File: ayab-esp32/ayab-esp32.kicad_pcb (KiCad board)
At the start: 2 copper layers, 57 parts, among them J501 USB_C_Receptacle_USB2.0, J601 VIN, Q201 AO3400A, Q502 AO3401A, Q603 AO3401A, U201 ESP32-S3-MINI-1, U301 ULN2003A, U302 ULN2003A, U303 ULN2003A, U501 SRV05-4, U601 XL1509, U602 XL1509, U701 SN74LVC4245

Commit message: add component selection, bom
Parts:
- removed Q603: AO3401A, ayab-esp32:SOT-23
- added BUZZER201: MLT-8530, easyeda2kicad:BUZ-SMD_4P-L8.5-W8.5-P8.50-BR, F.Cu at (-35.3, -30.9)
- added C201: 100n, Capacitor_SMD:C_0603_1608Metric, F.Cu at (221.6, -89.7)
- added C202: 100n, Capacitor_SMD:C_0603_1608Metric, F.Cu at (221.6, -87.2)
- added C203: 100n, Capacitor_SMD:C_0603_1608Metric, F.Cu at (221.6, -84.7)
- added C204: 100n, Capacitor_SMD:C_0603_1608Metric, F.Cu at (221.6, -82.1)
- added C205: 10u, Capacitor_SMD:C_0805_2012Metric, F.Cu at (229.8, -103.7)
- added C301: 100n, Capacitor_SMD:C_0603_1608Metric, F.Cu at (159.8, -100.4)
- added C302: 10u, Capacitor_SMD:C_0805_2012Metric, F.Cu at (159.9, -88.6)
- added C303: 10u, Capacitor_SMD:C_0805_2012Metric, F.Cu at (172.4, -88.6)
- added C304: 10u, Capacitor_SMD:C_0805_2012Metric, F.Cu at (147.4, -88.6)
- added C701: 100n, Capacitor_SMD:C_0603_1608Metric, F.Cu at (288.0, -95.0)
- added C702: 100n, Capacitor_SMD:C_0603_1608Metric, F.Cu at (292.8, -95.0)
- added C703: 100n, Capacitor_SMD:C_0603_1608Metric, F.Cu at (285.1, -73.5)
- added C704: 100n, Capacitor_SMD:C_0603_1608Metric, F.Cu at (285.1, -63.0)
- added D201: LED_YEL, Diode_SMD:D_0805_2012Metric, F.Cu at (215.3, -86.2)
- added D202: LED_GRN, Diode_SMD:D_0805_2012Metric, F.Cu at (215.3, -83.6)
- added D203: LED_RED, Diode_SMD:D_0805_2012Metric, F.Cu at (215.3, -81.0)
- added D204: SS54, Diode_SMD:D_SMA, F.Cu at (-36.5, -23.4)
- added D601: SS54, Diode_SMD:D_SMA, F.Cu at (397.3, -85.4)
- added FID101: Fiducial, Fiducial:Fiducial_0.5mm_Mask1.5mm, F.Cu at (82.2, -68.3)
- added FID102: Fiducial, Fiducial:Fiducial_0.5mm_Mask1.5mm, F.Cu at (82.2, -65.3)
- added FID103: Fiducial, Fiducial:Fiducial_0.5mm_Mask1.5mm, F.Cu at (82.2, -62.2)
- added H101: M3, MountingHole:MountingHole_2.2mm_M2_DIN965_Pad, F.Cu at (83.3, -77.9)
- added H102: M3, MountingHole:MountingHole_2.2mm_M2_DIN965_Pad, F.Cu at (83.3, -72.5)
- added H103: M3, MountingHole:MountingHole_2.2mm_M2_DIN965_Pad, F.Cu at (88.7, -77.9)
- added H104: M3, MountingHole:MountingHole_2.2mm_M2_DIN965_Pad, F.Cu at (88.7, -72.5)
- added H105: M3, MountingHole:MountingHole_2.2mm_M2_DIN965_Pad, F.Cu at (94.0, -77.9)
- added H106: M3, MountingHole:MountingHole_2.2mm_M2_DIN965_Pad, F.Cu at (94.0, -72.5)
- added H107: M3, MountingHole:MountingHole_2.2mm_M2_DIN965_Pad, F.Cu at (99.4, -77.9)
- added H108: M3, MountingHole:MountingHole_2.2mm_M2_DIN965_Pad, F.Cu at (99.4, -72.5)
- added J201: SPARE1, Connector_PinSocket_2.54mm:PinSocket_1x04_P2.54mm_Vertical, F.Cu at (-47.5, -33.9)
- added J202: SPARE0, Connector_PinSocket_2.54mm:PinSocket_1x04_P2.54mm_Vertical, F.Cu at (-42.9, -33.9)
- added J401: 900.965.CK35 SOLENOIDS A, easyeda2kicad:CONN-TH_CNJMA2004WV-10P, F.Cu at (-38.2, -61.1)
- added J402: 900.965.CK35 SOLENOIDS B, easyeda2kicad:CONN-TH_A2004WV-8P, F.Cu at (-40.2, -55.4)
- added J406: 930.940 SOLENOIDS A, Connector_JST:JST_XH_B10B-XH-A_1x10_P2.50mm_Vertical, F.Cu at (52.7, -77.2)
- added J407: 930.940 SOLENOIDS B, Connector_JST:JST_XH_B8B-XH-A_1x08_P2.50mm_Vertical, F.Cu at (52.7, -69.4)
- added J408: 910.950 EOL L, Connector_JST:JST_XH_B3B-XH-A_1x03_P2.50mm_Vertical, F.Cu at (69.6, -61.6)
- added J409: 930.940 EOL R, Connector_JST:JST_XH_B3B-XH-A_1x03_P2.50mm_Vertical, F.Cu at (69.6, -53.8)
- added J410: 930.940 ENCODERS, Connector_JST:JST_XH_B5B-XH-A_1x05_P2.50mm_Vertical, F.Cu at (52.7, -61.6)
- added J411: 900.965 EOL L, easyeda2kicad:CONN-TH_3P-P2.00_A2004WV-3P, F.Cu at (-31.9, -49.5)
- added J412: 900.965 EOL R, easyeda2kicad:CONN-TH_3P-P2.00_A2004WV-3P, F.Cu at (-31.9, -43.5)
- added J413: 900.965 ENCODERS, easyeda2kicad:CONN-TH_A2004WV-5P, F.Cu at (-43.2, -49.4)
- added J414: 930.940 EOL L, Connector_JST:JST_XH_B3B-XH-A_1x03_P2.50mm_Vertical, F.Cu at (-46.3, -42.6)
- added J701: CTRL_3v3, Connector_PinSocket_2.54mm:PinSocket_2x04_P2.54mm_Vertical, F.Cu at (271.8, -95.5)
- added J702: CTRL_5V, Connector_PinSocket_2.54mm:PinSocket_2x04_P2.54mm_Vertical, F.Cu at (301.8, -95.5)
- added J801: AYAB_UART, Connector_PinHeader_2.54mm:PinHeader_1x04_P2.54mm_Vertical, F.Cu at (299.0, -15.3)
- added J802: I2C_VBUS, Jumper:SolderJumper-3_P1.3mm_Bridged12_RoundedPad1.0x1.5mm, F.Cu at (217.0, -18.4)
- added J803: USER_I2C, Connector_JST:JST_SH_SM04B-SRSS-TB_1x04-1MP_P1.00mm_Horizontal, F.Cu at (219.1, -7.22)
- added J804: I2C_VBUS, Jumper:SolderJumper-3_P1.3mm_Bridged12_RoundedPad1.0x1.5mm, F.Cu at (157.1, -18.6)
- added J805: AYAB_SPI, Connector_JST:JST_SH_SM06B-SRSS-TB_1x06-1MP_P1.00mm_Horizontal, F.Cu at (260.1, -14.2)
- added J806: AYAB_I2C, Connector_PinSocket_2.54mm:PinSocket_1x04_P2.54mm_Vertical, F.Cu at (152.5, -18.6)
- added Q501: BCM857BV, Package_TO_SOT_SMD:SOT-363_SC-70-6, F.Cu at (157.6, -116.0)
- added Q601: BCM857BV, Package_TO_SOT_SMD:SOT-363_SC-70-6, F.Cu at (408.3, -85.7)
- added Q602: AO3401A, Package_TO_SOT_SMD:SOT-23, F.Cu at (411.3, -91.6)
- added Q801: AO3400A, Package_TO_SOT_SMD:SOT-23, F.Cu at (221.8, -18.5)
- added Q802: AO3400A, Package_TO_SOT_SMD:SOT-23, F.Cu at (221.8, -14.1)
- added Q803: AO3400A, Package_TO_SOT_SMD:SOT-23, F.Cu at (161.9, -18.7)
- added Q804: AO3400A, Package_TO_SOT_SMD:SOT-23, F.Cu at (161.9, -14.3)
- added R101: 5k1, Resistor_SMD:R_0603_1608Metric, F.Cu at (161.1, -126.2)
- added R102: 5k1, Resistor_SMD:R_0603_1608Metric, F.Cu at (163.7, -119.7)
- added R201: 10k, Resistor_SMD:R_0603_1608Metric, F.Cu at (221.6, -79.6)
- added R202: 5k1, Resistor_SMD:R_0603_1608Metric, F.Cu at (221.6, -77.1)
- added R203: 5k1, Resistor_SMD:R_0603_1608Metric, F.Cu at (225.6, -89.7)
- added R204: 5k1, Resistor_SMD:R_0603_1608Metric, F.Cu at (225.6, -87.2)
- added R205: 10k, Resistor_SMD:R_0603_1608Metric, F.Cu at (225.6, -84.7)
- added R206: 10k, Resistor_SMD:R_0603_1608Metric, F.Cu at (225.6, -82.1)
- added R207: 10k, Resistor_SMD:R_0603_1608Metric, F.Cu at (225.6, -79.6)
- added R208: 10k, Resistor_SMD:R_0603_1608Metric, F.Cu at (225.6, -77.1)
- added R209: 5k1, Resistor_SMD:R_0603_1608Metric, F.Cu at (229.6, -89.7)
- added R210: 5k1, Resistor_SMD:R_0603_1608Metric, F.Cu at (229.6, -87.2)
- added R211: 10k, Resistor_SMD:R_0603_1608Metric, F.Cu at (229.6, -84.7)
- added R212: 0R, Resistor_SMD:R_0603_1608Metric, F.Cu at (229.6, -82.1)
- added R502: 65k, Resistor_SMD:R_0603_1608Metric, F.Cu at (154.6, -115.1)
- added R503: 65k, Resistor_SMD:R_0603_1608Metric, F.Cu at (154.6, -116.8)
- added R601: 65k, Resistor_SMD:R_0603_1608Metric, F.Cu at (411.7, -97.1)
- added R611: 0R, Resistor_SMD:R_0603_1608Metric, F.Cu at (-22.5, -49.6)
- added R701: 10k, Resistor_SMD:R_0603_1608Metric, F.Cu at (310.9, -94.4)
- added R702: 10k, Resistor_SMD:R_0603_1608Metric, F.Cu at (307.9, -94.4)
- added R703: 10k, Resistor_SMD:R_0603_1608Metric, F.Cu at (310.9, -96.0)
- added R704: 10k, Resistor_SMD:R_0603_1608Metric, F.Cu at (307.9, -96.0)
- added R705: 10k, Resistor_SMD:R_0603_1608Metric, F.Cu at (310.9, -97.7)
- added R706: 10k, Resistor_SMD:R_0603_1608Metric, F.Cu at (307.9, -97.7)
- added R707: 10k, Resistor_SMD:R_0603_1608Metric, F.Cu at (310.9, -99.3)
- added R708: 10k, Resistor_SMD:R_0603_1608Metric, F.Cu at (307.9, -99.3)
- added R709: 10k, Resistor_SMD:R_0603_1608Metric, F.Cu at (310.9, -100.9)
- added R710: 10k, Resistor_SMD:R_0603_1608Metric, F.Cu at (307.9, -100.9)
- added R711: 10k, Resistor_SMD:R_0603_1608Metric, F.Cu at (310.9, -102.5)
- added R712: 10k, Resistor_SMD:R_0603_1608Metric, F.Cu at (307.9, -102.5)
- added R713: 10k, Resistor_SMD:R_0603_1608Metric, F.Cu at (310.9, -104.2)
- added R714: 10k, Resistor_SMD:R_0603_1608Metric, F.Cu at (307.9, -104.2)
- added R715: 100k, Resistor_SMD:R_0603_1608Metric, F.Cu at (274.4, -73.5)
- added R716: 100k, Resistor_SMD:R_0603_1608Metric, F.Cu at (283.5, -73.5)
- added R717: 100k, Resistor_SMD:R_0603_1608Metric, F.Cu at (274.4, -63.0)
- added R718: 100k, Resistor_SMD:R_0603_1608Metric, F.Cu at (283.5, -63.0)
- added R719: 10k, Resistor_SMD:R_0603_1608Metric, F.Cu at (272.9, -73.5)
- added R720: 10k, Resistor_SMD:R_0603_1608Metric, F.Cu at (283.5, -70.5)
- added R721: 10k, Resistor_SMD:R_0603_1608Metric, F.Cu at (272.9, -63.0)
- added R722: 10k, Resistor_SMD:R_0603_1608Metric, F.Cu at (283.5, -59.9)
- added R723: 4k7, Resistor_SMD:R_0603_1608Metric, F.Cu at (286.6, -73.5)
- added R724: 1k, Resistor_SMD:R_0603_1608Metric, F.Cu at (285.1, -70.5)
- added R725: 4k7, Resistor_SMD:R_0603_1608Metric, F.Cu at (286.6, -63.0)
- added R726: 1k, Resistor_SMD:R_0603_1608Metric, F.Cu at (285.1, -59.9)
- added R727: 3k3, Resistor_SMD:R_0603_1608Metric, F.Cu at (271.3, -73.5)
- added R728: 4k7, Resistor_SMD:R_0603_1608Metric, F.Cu at (271.3, -70.5)
- added R729: 3k3, Resistor_SMD:R_0603_1608Metric, F.Cu at (271.4, -63.0)
- added R730: 4k7, Resistor_SMD:R_0603_1608Metric, F.Cu at (271.4, -59.9)
- added R731: 22k, Resistor_SMD:R_0603_1608Metric, F.Cu at (274.4, -70.5)
- added R732: 22k, Resistor_SMD:R_0603_1608Metric, F.Cu at (274.4, -59.9)
- added R733: 47k, Resistor_SMD:R_0603_1608Metric, F.Cu at (272.9, -70.5)
- added R734: 47k, Resistor_SMD:R_0603_1608Metric, F.Cu at (272.9, -59.9)
- added R801: 47R, Resistor_SMD:R_0603_1608Metric, F.Cu at (212.7, -19.5)
- added R802: 47R, Resistor_SMD:R_0603_1608Metric, F.Cu at (212.7, -17.0)
- added R803: 5k1, Resistor_SMD:R_0603_1608Metric, F.Cu at (212.7, -14.5)
- added R804: 5k1, Resistor_SMD:R_0603_1608Metric, F.Cu at (212.7, -11.9)
- added R805: 47R, Resistor_SMD:R_0603_1608Metric, F.Cu at (303.3, -16.3)
- added R806: 47R, Resistor_SMD:R_0603_1608Metric, F.Cu at (303.3, -13.8)
- added R807: 5k1, Resistor_SMD:R_0603_1608Metric, F.Cu at (212.7, -9.44)
- added R808: 5k1, Resistor_SMD:R_0603_1608Metric, F.Cu at (212.7, -6.92)
- added R809: 47R, Resistor_SMD:R_0603_1608Metric, F.Cu at (148.2, -19.7)
- added R810: 47R, Resistor_SMD:R_0603_1608Metric, F.Cu at (148.2, -17.2)
- added R811: 5k1, Resistor_SMD:R_0603_1608Metric, F.Cu at (148.2, -14.7)
- added R812: 5k1, Resistor_SMD:R_0603_1608Metric, F.Cu at (148.2, -12.2)
- added R813: 47R, Resistor_SMD:R_0603_1608Metric, F.Cu at (267.5, -16.8)
- added R814: 10k, Resistor_SMD:R_0603_1608Metric, F.Cu at (267.5, -14.3)
- added R815: 10k, Resistor_SMD:R_0603_1608Metric, F.Cu at (267.5, -11.8)
- added R816: 5k1, Resistor_SMD:R_0603_1608Metric, F.Cu at (148.2, -9.66)
- added R817: 5k1, Resistor_SMD:R_0603_1608Metric, F.Cu at (148.2, -7.15)
- added SW201: USER, matei:TS-1187A-B-A-B, F.Cu at (222.9, -106.7)
- added SW202: RESET, matei:TS-1187A-B-A-B, F.Cu at (223.6, -100.3)
- added SW203: BOOTSEL, matei:TS-1187A-B-A-B, F.Cu at (223.6, -94.1)
- added TP301: MCP_INTA, TestPoint:TestPoint_Pad_D2.0mm, F.Cu at (154.2, -100.6)
- added TP302: MCP_INTB, TestPoint:TestPoint_Pad_D2.0mm, F.Cu at (157.4, -100.6)
- added TP401: 9, TestPoint:TestPoint_Pad_D2.0mm, F.Cu at (51.2, -55.1)
- added TP402: 10, TestPoint:TestPoint_Pad_D2.0mm, F.Cu at (51.2, -51.1)
- added TP501: USB_BUSV, TestPoint:TestPoint_Pad_D2.0mm, F.Cu at (-26.0, -34.2)
- added TP502: USBM, TestPoint:TestPoint_Pad_D2.0mm, F.Cu at (-26.0, -30.1)
- added TP503: USBP, TestPoint:TestPoint_Pad_D2.0mm, F.Cu at (-26.0, -26.1)
- added TP701: CMP-L, TestPoint:TestPoint_Pad_D2.0mm, F.Cu at (-22.5, -61.5)
- added TP702: CMP-L, TestPoint:TestPoint_Pad_D2.0mm, F.Cu at (-22.5, -57.4)
- added U304: ULN2003A, Package_SO:SOIC-16_3.9x9.9mm_P1.27mm, F.Cu at (153.6, -90.6)
- added U702: LM393, Package_SO:SOIC-8_3.9x4.9mm_P1.27mm, F.Cu at (279.0, -72.3)
- added U703: LM393, Package_SO:SOIC-8_3.9x4.9mm_P1.27mm, F.Cu at (279.0, -61.8)
- added kibuzzard-64F67C37: G***, kibuzzard-64F67C37, F.Cu at (266.8, -103.0)
- added kibuzzard-64F67C8E: G***, kibuzzard-64F67C8E, F.Cu at (266.9, -100.5)
- added kibuzzard-64F67C97: G***, kibuzzard-64F67C97, F.Cu at (267.5, -98.0)
- added kibuzzard-64F67CA0: G***, kibuzzard-64F67CA0, F.Cu at (268.1, -95.5)
- added kibuzzard-64F67CA5: G***, kibuzzard-64F67CA5, F.Cu at (278.0, -95.5)
- added kibuzzard-64F67CAF: G***, kibuzzard-64F67CAF, F.Cu at (279.4, -98.0)
- added kibuzzard-64F67CB8: G***, kibuzzard-64F67CB8, F.Cu at (279.5, -100.5)
- added kibuzzard-64F68412: G***, kibuzzard-64F68412, F.Cu at (273.1, -106.2)
- added kibuzzard-64F68422: G***, kibuzzard-64F68422, F.Cu at (303.1, -106.2)
- C501, C502: footprint ayab-esp32:C_0402_1005Metric -> Capacitor_SMD:C_0603_1608Metric
- C601, C602, C603, C604, C605, C610, C616, C617, C618, C619, C620, C621: footprint ayab-esp32:C_0603_1608Metric -> Capacitor_SMD:C_0805_2012Metric
- C606, C607, C608, C612, C613: footprint ayab-esp32:CP_Elec_8x10.5 -> Capacitor_THT:CP_Radial_D6.3mm_P2.50mm
- C609: value 220uF -> 220u; footprint ayab-esp32:CP_Elec_8x10.5 -> Capacitor_THT:CP_Radial_D6.3mm_P2.50mm
- C611: value 10uF -> 10u; footprint ayab-esp32:C_0603_1608Metric -> Capacitor_SMD:C_0805_2012Metric
- C614, C615: footprint ayab-esp32:C_0603_1608Metric -> Capacitor_SMD:C_0603_1608Metric
- D602, D603, D604: footprint ayab-esp32:D_0603_1608Metric -> Diode_SMD:D_0603_1608Metric
- D605, D606: footprint ayab-esp32:D_SMA -> Diode_SMD:D_SMA
- J501: footprint ayab-esp32:USB_C_Receptacle_HRO_TYPE-C-31-M-12 -> Connector_USB:USB_C_Receptacle_HRO_TYPE-C-31-M-12
- J601: footprint ayab-esp32:DC-IN-TH_DC-005-5A-2.0-SMT -> easyeda2kicad:DC-IN-TH_DC-005-5A-2.0-SMT
- JP501: footprint ayab-esp32:SolderJumper-2_P1.3mm_Bridged_RoundedPad1.0x1.5mm -> Jumper:SolderJumper-2_P1.3mm_Bridged_RoundedPad1.0x1.5mm
- L601, L602: footprint ayab-esp32:L_12x12mm_H8mm -> Inductor_SMD:L_12x12mm_H8mm
- Q201, Q502: footprint ayab-esp32:SOT-23 -> Package_TO_SOT_SMD:SOT-23
- R501: footprint ayab-esp32:R_0402_1005Metric -> Resistor_SMD:R_0603_1608Metric
- R602, R607: footprint ayab-esp32:R_0603_1608Metric -> Resistor_SMD:R_0603_1608Metric
- R603: value 65k -> 12k; footprint ayab-esp32:R_0603_1608Metric -> Resistor_SMD:R_0603_1608Metric
- R604: value 12k -> 5k1; footprint ayab-esp32:R_0603_1608Metric -> Resistor_SMD:R_0603_1608Metric
- R605: value 5k -> 3k3; footprint ayab-esp32:R_0603_1608Metric -> Resistor_SMD:R_0603_1608Metric
- R606: value 3k3 -> 1k; footprint ayab-esp32:R_0603_1608Metric -> Resistor_SMD:R_0603_1608Metric
- R608: value 1k -> 3k3; footprint ayab-esp32:R_0603_1608Metric -> Resistor_SMD:R_0603_1608Metric
- R609: value 3k3 -> 1k8; footprint ayab-esp32:R_0603_1608Metric -> Resistor_SMD:R_0603_1608Metric
- R610: value 1k8 -> 0R; footprint ayab-esp32:R_0603_1608Metric -> Resistor_SMD:R_0603_1608Metric
- TP601, TP602, TP603: footprint ayab-esp32:TestPoint_Pad_D1.0mm -> TestPoint:TestPoint_Pad_D2.0mm
- U201: footprint ayab-esp32:ESP32-S3-MINI-1 -> Espressif:ESP32-S3-MINI-1
- U301: value ULN2003A -> MCP23017_SS; footprint ayab-esp32:SOIC-16_3.9x9.9mm_P1.27mm -> Package_SO:SSOP-28_5.3x10.2mm_P0.65mm
- U302, U303: footprint ayab-esp32:SOIC-16_3.9x9.9mm_P1.27mm -> Package_SO:SOIC-16_3.9x9.9mm_P1.27mm
- U501: footprint ayab-esp32:SOT-23-6 -> Package_TO_SOT_SMD:SOT-23-6
- U601, U602: footprint ayab-esp32:SOIC-8_3.9x4.9mm_P1.27mm -> Package_SO:SOIC-8_3.9x4.9mm_P1.27mm
- U701: footprint ayab-esp32:TSSOP-24_4.4x6.5mm_P0.5mm -> Package_SO:TSSOP-24_4.4x6.5mm_P0.5mm
- moved R602 397.9 mm to (411.7, -94.6)
- moved TP601 390.5 mm to (411.7, -100.4)
- moved J601 383.5 mm to (401.9, -95.0)
- moved C612 336.3 mm to (331.5, -90.1)
- moved C608 331.5 mm to (331.5, -100.1)
- moved C617 325.3 mm to (301.5, -123.9), turned to 90 degrees
- moved C615 318.5 mm to (296.9, -123.9), turned to -90 degrees
- moved C621 316.6 mm to (298.4, -123.9), turned to 90 degrees
- moved C611 316.6 mm to (294.0, -129.3), turned to -90 degrees
- moved C613 316.4 mm to (331.1, -34.9)
- moved C619 314.6 mm to (299.9, -123.9), turned to 90 degrees
- moved R609 314.4 mm to (295.3, -123.9), turned to -90 degrees
- moved C609 312.8 mm to (331.1, -44.9)
- moved L602 312.7 mm to (308.9, -128.2), turned to -90 degrees
- moved R607 310.0 mm to (293.8, -123.9), turned to 90 degrees
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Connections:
- C612 pad 1: +5V -> /PSU/5V_SW
- C613 pad 1: +3V3 -> /PSU/5V_SW
- C614 pad 2: +5V -> /PSU/5V_SW
- C615 pad 2: +3V3 -> /PSU/5V_SW
- C616 pad 1: +5V -> /PSU/5V_SW
- C617 pad 1: +3V3 -> /PSU/5V_SW
- C618 pad 1: +5V -> /PSU/5V_SW
- C619 pad 1: +3V3 -> /PSU/5V_SW
- C620 pad 1: +5V -> /PSU/5V_SW
- C621 pad 1: +3V3 -> /PSU/5V_SW
- L601 pad 2: +5V -> /PSU/5V_SW
- L602 pad 2: +3V3 -> /PSU/5V_SW
- R603 pad 1: Net-(Q602B-C2) -> +12V
- R603 pad 2: GND -> Net-(D602-A)
- R604 pad 1: +12V -> +5V
- R604 pad 2: Net-(D602-A) -> Net-(D603-A)
- R605 pad 1: +5V -> +3V3
- R605 pad 2: Net-(D603-A) -> Net-(D604-A)
- R606 pad 1: +3V3 -> Net-(U601-FB)
- R606 pad 2: Net-(D604-A) -> GND
- R607 pad 1: Net-(U601-FB) -> Net-(U602-FB)
- R608 pad 1: Net-(U602-FB) -> Net-(U601-FB)
- R608 pad 2: GND -> /PSU/5V_SW
- R609 pad 1: Net-(U601-FB) -> Net-(U602-FB)
- R609 pad 2: +5V -> /PSU/5V_SW
- R610 pad 1: Net-(U602-FB) -> /PSU/5V_SW
- TP602 pad 1: +5V -> /PSU/5V_SW
- TP603 pad 1: +3V3 -> /PSU/5V_SW
- U201 pad 10: /ESP32/MCU_SOL_2 -> /ESP32/ENC_B
- U201 pad 11: /ESP32/MCU_SOL_3 -> /ESP32/ENC_BP
- U201 pad 12: /ESP32/MCU_SOL_8 -> /AUX-CONNECTORS/AYAB_SDA
- U201 pad 13: /ESP32/MCU_SOL_9 -> /AUX-CONNECTORS/AYAB_SCL
- U201 pad 14: /ESP32/MCU_SOL_A -> /AUX-CONNECTORS/AYAB_CS
- U201 pad 15: /ESP32/MCU_SOL_B -> /AUX-CONNECTORS/AYAB_CIPO
- U201 pad 16: /ESP32/MCU_SOL_C -> /AUX-CONNECTORS/AYAB_COPI
- U201 pad 17: /ESP32/MCU_SOL_D -> /AUX-CONNECTORS/AYAB_SCK
- U201 pad 18: /ESP32/MCU_SOL_E -> /ESP32/ESP14
- U201 pad 19: /ESP32/MCU_SOL_4 -> /AUX-CONNECTORS/I2C_SDA
- U201 pad 20: /ESP32/MCU_SOL_5 -> /AUX-CONNECTORS/I2C_SCL
- U201 pad 21: /ESP32/MCU_SOL_6 -> /ESP32/ESP17
- U201 pad 22: /ESP32/MCU_SOL_7 -> /ESP32/ESP18
- U201 pad 25: /ESP32/MCU_SOL_F -> /ESP32/ESP21
- U201 pad 27: /ESP32/EOL_R_P -> unconnected-(U201-GPIO47/SPICLK_P/SUBSPICLK_P_DIFF-Pad27)
- U201 pad 28: /ESP32/EOL_R_N -> Net-(D203-K)
- U201 pad 29: /CONNECTORS/I2C_SDA -> Net-(D202-K)
- U201 pad 30: /CONNECTORS/I2C_SCL -> unconnected-(U201-GPIO48/SPICLK_N/SUBSPICLK_N_DIFF-Pad30)
- U201 pad 31: /ESP32/ENC_A -> Net-(D201-K)
- U201 pad 32: /ESP32/ENC_B -> Net-(U201-SPIIO7/GPIO36/FSPICLK/SUBSPICLK)
- U201 pad 33: /ESP32/ENC_BP -> unconnected-(U201-SPIDQS/GPIO37/FSPIQ/SUBSPIQ-Pad33)
- U201 pad 35: /CONNECTORS/SPI_SCK -> /ESP32/ESP39
- U201 pad 36: /CONNECTORS/SPI_COPI -> /ESP32/ESP40
- U201 pad 37: /CONNECTORS/SPI_CIPO -> /ESP32/ESP41
- U201 pad 38: /CONNECTORS/SPI_CS -> /ESP32/ESP42
- U201 pad 39: /CONNECTORS/UART_TX -> /AUX-CONNECTORS/UART_TX
- U201 pad 40: /CONNECTORS/UART_RX -> /AUX-CONNECTORS/UART_RX
- U201 pad 7: unconnected-(U201-GPIO3/TOUCH3/ADC1_CH2-Pad7) -> /ESP32/EOL_R_P
- U201 pad 8: /ESP32/MCU_SOL_0 -> /ESP32/EOL_R_N
- U201 pad 9: /ESP32/MCU_SOL_1 -> /ESP32/ENC_A
- U301 pad 1: /ESP32/MCU_SOL_6 -> /SOLENOID DRIVERS/MCU_SOL_7
- U301 pad 10: /CONNECTORS/SOL_0 -> GND
- U301 pad 11: /CONNECTORS/SOL_1 -> unconnected-(U301-NC-Pad11)
- U301 pad 12: /CONNECTORS/SOL_2 -> /AUX-CONNECTORS/AYAB_SCL
- U301 pad 13: /CONNECTORS/SOL_3 -> /AUX-CONNECTORS/AYAB_SDA
- U301 pad 14: /CONNECTORS/SOL_4 -> unconnected-(U301-NC-Pad14)
- U301 pad 15: /CONNECTORS/SOL_5 -> GND
- U301 pad 16: /CONNECTORS/SOL_6 -> GND
- U301 pad 2: /ESP32/MCU_SOL_5 -> /SOLENOID DRIVERS/MCU_SOL_6
- U301 pad 3: /ESP32/MCU_SOL_4 -> /SOLENOID DRIVERS/MCU_SOL_5
- U301 pad 4: /ESP32/MCU_SOL_3 -> /SOLENOID DRIVERS/MCU_SOL_4
- U301 pad 5: /ESP32/MCU_SOL_2 -> /SOLENOID DRIVERS/MCU_SOL_3
- U301 pad 6: /ESP32/MCU_SOL_1 -> /SOLENOID DRIVERS/MCU_SOL_2
- U301 pad 7: /ESP32/MCU_SOL_0 -> /SOLENOID DRIVERS/MCU_SOL_1
- U301 pad 8: GND -> /SOLENOID DRIVERS/MCU_SOL_0
- U301 pad 9: +12V -> +3V3
- U302 pad 1: /ESP32/MCU_SOL_D -> /SOLENOID DRIVERS/MCU_SOL_7
- U302 pad 10: /CONNECTORS/SOL_7 -> /BROTHER-CONNECTORS/SOL_1
- U302 pad 11: /CONNECTORS/SOL_8 -> /BROTHER-CONNECTORS/SOL_2
- U302 pad 12: /CONNECTORS/SOL_9 -> /BROTHER-CONNECTORS/SOL_3
- U302 pad 13: /CONNECTORS/SOL_A -> /BROTHER-CONNECTORS/SOL_4
- U302 pad 14: /CONNECTORS/SOL_B -> /BROTHER-CONNECTORS/SOL_5
- U302 pad 15: /CONNECTORS/SOL_C -> /BROTHER-CONNECTORS/SOL_6
- U302 pad 16: /CONNECTORS/SOL_D -> /BROTHER-CONNECTORS/SOL_7
- U302 pad 2: /ESP32/MCU_SOL_C -> /SOLENOID DRIVERS/MCU_SOL_6
- U302 pad 3: /ESP32/MCU_SOL_B -> /SOLENOID DRIVERS/MCU_SOL_5
- U302 pad 4: /ESP32/MCU_SOL_A -> /SOLENOID DRIVERS/MCU_SOL_4
- U302 pad 5: /ESP32/MCU_SOL_9 -> /SOLENOID DRIVERS/MCU_SOL_3
- U302 pad 6: /ESP32/MCU_SOL_8 -> /SOLENOID DRIVERS/MCU_SOL_2
- U302 pad 7: /ESP32/MCU_SOL_7 -> /SOLENOID DRIVERS/MCU_SOL_1
- U303 pad 1: /ESP32/MCU_SOL_F -> /SOLENOID DRIVERS/MCU_SOL_0
- U303 pad 10: unconnected-(U303-O7-Pad10) -> /BROTHER-CONNECTORS/SOL_F
- U303 pad 15: /CONNECTORS/SOL_E -> unconnected-(U303-O2-Pad15)
- U303 pad 16: /CONNECTORS/SOL_F -> /BROTHER-CONNECTORS/SOL_0
- U303 pad 2: /ESP32/MCU_SOL_E -> unconnected-(U303-I2-Pad2)
- U303 pad 7: unconnected-(U303-I7-Pad7) -> /SOLENOID DRIVERS/MCU_SOL_F
- U501 pad 4: unconnected-(U501-IO3-Pad4) -> /ESP32/USB_P
- U501 pad 6: unconnected-(U501-IO4-Pad6) -> /ESP32/USB_M
- U701 pad 10: unconnected-(U701-A8-Pad10) -> Net-(J702-Pin_8)
- U701 pad 14: unconnected-(U701-B8-Pad14) -> Net-(J701-Pin_8)
- U701 pad 3: /CONNECTORS/ENC_V1 -> /BROTHER-CONNECTORS/ENC_V1
- U701 pad 4: /CONNECTORS/ENC_V2 -> /BROTHER-CONNECTORS/ENC_V2
- U701 pad 5: /CONNECTORS/ENC_BELTPHASE -> /BROTHER-CONNECTORS/ENC_BELTPHASE
- U701 pad 8: /IO CONDITIONING/EOL_R_K -> /BROTHER-CONNECTORS/EOL_R_N
- U701 pad 9: /IO CONDITIONING/EOL_R_L -> /BROTHER-CONNECTORS/EOL_R_S
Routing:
- net /SOLENOID DRIVERS/MCU_SOL_7: track 0.00 -> 22.6 mm
- net /BROTHER-CONNECTORS/EOL_R_S: track 0.00 -> 22.0 mm
- net /SOLENOID DRIVERS/MCU_SOL_6: track 0.00 -> 21.9 mm
- net /SOLENOID DRIVERS/MCU_SOL_5: track 0.00 -> 21.4 mm
- net /BROTHER-CONNECTORS/EOL_R_N: track 0.00 -> 21.1 mm
- net /IO CONDITIONING/EOL_L_L: track 0.00 -> 21.0 mm
- net /SOLENOID DRIVERS/MCU_SOL_4: track 0.00 -> 20.7 mm
- net /SOLENOID DRIVERS/MCU_SOL_3: track 0.00 -> 20.1 mm
- net /IO CONDITIONING/EOL_L_K: track 0.00 -> 20.1 mm
- net GND: track 0.00 -> 19.9 mm, vias 0 -> 1
- net /SOLENOID DRIVERS/MCU_SOL_8: track 0.00 -> 19.6 mm
- net /SOLENOID DRIVERS/MCU_SOL_2: track 0.00 -> 19.5 mm
- net /SOLENOID DRIVERS/MCU_SOL_9: track 0.00 -> 18.9 mm
- net /SOLENOID DRIVERS/MCU_SOL_1: track 0.00 -> 18.8 mm
- net /BROTHER-CONNECTORS/ENC_V1: track 0.00 -> 18.8 mm
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- added copper zone on F.Cu, net +3V3
- added copper zone on F.Cu, net +5V
- added copper zone on F.Cu, net GND
- added copper zone on F.Cu, net Net-(D605-K)
- added copper zone on F.Cu, net Net-(D606-K)

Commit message: first draft layout DRC clean
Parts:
- removed JP501: USB5V, Jumper:SolderJumper-2_P1.3mm_Bridged_RoundedPad1.0x1.5mm
- removed Q601: BCM857BV, Package_TO_SOT_SMD:SOT-363_SC-70-6
- removed Q602: AO3401A, Package_TO_SOT_SMD:SOT-23
- removed R601, R602: 65k, Resistor_SMD:R_0603_1608Metric
- removed kibuzzard-64F67C37: G***, kibuzzard-64F67C37
- removed kibuzzard-64F67C8E: G***, kibuzzard-64F67C8E
- removed kibuzzard-64F67C97: G***, kibuzzard-64F67C97
- removed kibuzzard-64F67CA0: G***, kibuzzard-64F67CA0
- removed kibuzzard-64F67CA5: G***, kibuzzard-64F67CA5
- removed kibuzzard-64F67CAF: G***, kibuzzard-64F67CAF
- removed kibuzzard-64F67CB8: G***, kibuzzard-64F67CB8
- removed kibuzzard-64F68422: G***, kibuzzard-64F68422
- added C305: 100n, Capacitor_SMD:C_0603_1608Metric, F.Cu at (117.8, 125.7)
- added FID104: Fiducial, Fiducial:Fiducial_1mm_Mask2mm, F.Cu at (207.0, 124.9)
- added FID105: Fiducial, Fiducial:Fiducial_1mm_Mask2mm, F.Cu at (194.2, 150.8)
- added FID106: Fiducial, Fiducial:Fiducial_1mm_Mask2mm, F.Cu at (266.5, 153.0)
- added G***: LOGO, LOGO, F.Cu at (160.5, 134.2)
- added J403: 910.950 SOLENOIDS A, Library:HNC2-2.5P-10DS, F.Cu at (129.4, 147.5)
- added J404: 910.950 SOLENOIDS B, Library:HNC2-2.5P-8DS, F.Cu at (93.5, 147.4)
- added J405: 910.950 ENCODERS EOL R, Library:HNC2-2.5P-10DS, F.Cu at (173.4, 147.5)
- added J602: Brother_5P, Library:Brother_5P, F.Cu at (45.5, 130.2)
- added J603: Brother_4P, Library:Brother_4P, F.Cu at (54.0, 130.2)
- added R504: 0R, Resistor_SMD:R_0603_1608Metric, F.Cu at (255.2, 154.0)
- added REF**: OSHW-Logo2_14.6x12mm_SilkScreen, Symbol:OSHW-Logo2_14.6x12mm_SilkScreen, F.Cu at (292.5, 141.9)
- added kibuzzard-658236A5: G***, kibuzzard-658236A5, F.Cu at (208.7, 152.3)
- added kibuzzard-658236BF: G***, kibuzzard-658236BF, F.Cu at (207.5, 154.8)
- added kibuzzard-658236C5: G***, kibuzzard-658236C5, F.Cu at (207.4, 157.3)
- added kibuzzard-658236E5: G***, kibuzzard-658236E5, F.Cu at (220.4, 157.4)
- added kibuzzard-658236F2: G***, kibuzzard-658236F2, F.Cu at (219.8, 154.9)
- added kibuzzard-658236FD: G***, kibuzzard-658236FD, F.Cu at (219.2, 152.4)
- added kibuzzard-65823743: G***, kibuzzard-65823743, F.Cu at (220.5, 159.9)
- added kibuzzard-6583399A: G***, kibuzzard-6583399A, F.Cu at (107.9, 119.6)
- added kibuzzard-65834FF6: G***, kibuzzard-65834FF6, F.Cu at (139.7, 119.8)
- added kibuzzard-6583500B: G***, kibuzzard-6583500B, F.Cu at (121.3, 119.8)
- added kibuzzard-659A3543: G***, kibuzzard-659A3543, F.Cu at (159.8, 119.7)
- added kibuzzard-659B56F0: G***, kibuzzard-659B56F0, F.Cu at (151.0, 154.4)
- added kibuzzard-659B572C: G***, kibuzzard-659B572C, F.Cu at (151.2, 160.0)
- added kibuzzard-659B5818: G***, kibuzzard-659B5818, F.Cu at (322.2, 140.4)
- added kibuzzard-659B5831: G***, kibuzzard-659B5831, F.Cu at (322.4, 146.2)
- added kibuzzard-659B5873: G***, kibuzzard-659B5873, F.Cu at (83.7, 159.7)
- added kibuzzard-659B5892: G***, kibuzzard-659B5892, F.Cu at (82.8, 154.0)
- added kibuzzard-659B590F: G***, kibuzzard-659B590F, F.Cu at (137.3, 160.2)
- added kibuzzard-659B5942: G***, kibuzzard-659B5942, F.Cu at (141.8, 154.1)
- added kibuzzard-659B5A24: G***, kibuzzard-659B5A24, F.Cu at (77.7, 140.1)
- added kibuzzard-659B5A5E: G***, kibuzzard-659B5A5E, F.Cu at (75.3, 146.4)
- added kibuzzard-659F41CB: G***, kibuzzard-659F41CB, F.Cu at (269.9, 160.2)
- added kibuzzard-659F42B8: G***, kibuzzard-659F42B8, F.Cu at (128.2, 144.1)
- added kibuzzard-659F42CC: G***, kibuzzard-659F42CC, F.Cu at (93.5, 144.1)
- added kibuzzard-659F44B0: G***, kibuzzard-659F44B0, F.Cu at (69.3, 124.3)
- added kibuzzard-659F49E4: G***, kibuzzard-659F49E4, F.Cu at (304.7, 134.5)
- added kibuzzard-659F49F4: G***, kibuzzard-659F49F4, F.Cu at (271.6, 134.5)
- added kibuzzard-65A1AC88: G***, kibuzzard-65A1AC88, F.Cu at (77.8, 135.0)
- added kibuzzard-65A1ADEE: G***, kibuzzard-65A1ADEE, F.Cu at (309.4, 145.3)
- added kibuzzard-65A1DFCB: G***, kibuzzard-65A1DFCB, F.Cu at (209.3, 142.5)
- added kibuzzard-65A20B9D: G***, kibuzzard-65A20B9D, F.Cu at (71.2, 159.7)
- added kibuzzard-65A2E096: G***, kibuzzard-65A2E096, F.Cu at (170.7, 124.8)
- added kibuzzard-65A2E0AA: G***, kibuzzard-65A2E0AA, F.Cu at (182.3, 124.8)
- added kibuzzard-65A2E6F1: G***, kibuzzard-65A2E6F1, F.Cu at (255.8, 124.8)
- added kibuzzard-65A2F3CF: G***, kibuzzard-65A2F3CF, F.Cu at (172.2, 144.1)
- added kibuzzard-65A3FDB9: G***, kibuzzard-65A3FDB9, F.Cu at (54.8, 158.2)
- added kibuzzard-65A3FDD0: G***, kibuzzard-65A3FDD0, F.Cu at (63.3, 151.4)
- D601: value SS54 -> KMB14F; footprint Diode_SMD:D_SMA -> easyeda2kicad:MBF-SMD_L4.8-W3.8-P2.54-LS6.8-TL
- FID101, FID102, FID103: footprint Fiducial:Fiducial_0.5mm_Mask1.5mm -> Fiducial:Fiducial_1mm_Mask2mm
- J201, J202, J806: footprint Connector_PinSocket_2.54mm:PinSocket_1x04_P2.54mm_Vertical -> Connector_PinHeader_2.54mm:PinHeader_1x04_P2.54mm_Horizontal
- J401: footprint easyeda2kicad:CONN-TH_CNJMA2004WV-10P -> Library:530141010
- J402: footprint easyeda2kicad:CONN-TH_A2004WV-8P -> Library:530140810
- J406: footprint Connector_JST:JST_XH_B10B-XH-A_1x10_P2.50mm_Vertical -> Library:SHDR10W70P0X250_1X10_2740X490X590P
- J407: footprint Connector_JST:JST_XH_B8B-XH-A_1x08_P2.50mm_Vertical -> Library:SHDR8W65P0X250_1X8_2240X490X610P
- J408: footprint Connector_JST:JST_XH_B3B-XH-A_1x03_P2.50mm_Vertical -> Library:HNC2-2.5P-3DS
- J409, J414: footprint Connector_JST:JST_XH_B3B-XH-A_1x03_P2.50mm_Vertical -> easyeda2kicad:CONN-TH_3P-P2.50_X2564WV-03-N0SN
- J410: footprint Connector_JST:JST_XH_B5B-XH-A_1x05_P2.50mm_Vertical -> easyeda2kicad:CONN-TH_X2564WV-05-N0SN
- J411, J412: footprint easyeda2kicad:CONN-TH_3P-P2.00_A2004WV-3P -> Library:CONN-TH_3P-P2.00_A2004WV-3P
- J413: footprint easyeda2kicad:CONN-TH_A2004WV-5P -> Library:530140510
- J701, J702: footprint Connector_PinSocket_2.54mm:PinSocket_2x04_P2.54mm_Vertical -> Connector_PinHeader_2.54mm:PinHeader_2x04_P2.54mm_Vertical
- J801: footprint Connector_PinHeader_2.54mm:PinHeader_1x04_P2.54mm_Vertical -> Connector_PinHeader_2.54mm:PinHeader_1x04_P2.54mm_Horizontal
- Q502: value AO3401A -> LP9435LT1G
- R502: value 65k -> 100k
- R503: value 65k -> 68k
- SW201, SW202, SW203: footprint matei:TS-1187A-B-A-B -> easyeda2kicad:KEY-TH_4P-L7.5-W11.5-P4.5
- TP301, TP302, TP401, TP402, TP501, TP502, TP503, TP601, TP602, TP603, TP701: footprint TestPoint:TestPoint_Pad_D2.0mm -> TestPoint:TestPoint_Pad_D1.0mm
- TP702: value CMP-L -> CMP-R; footprint TestPoint:TestPoint_Pad_D2.0mm -> TestPoint:TestPoint_Pad_D1.0mm
- moved J412 408.0 mm to (329.6, 145.7)
- moved C607 407.7 mm to (327.4, 160.7), turned to 90 degrees
- moved R603 392.7 mm to (332.8, 162.0)
- moved TP702 391.9 mm to (312.9, 145.3)
- moved D602 386.3 mm to (335.9, 162.0), turned to 180 degrees
- moved R611 380.4 mm to (310.1, 134.9)
- moved C606 369.3 mm to (301.4, 121.7), turned to 180 degrees
- moved R610 353.1 mm to (276.9, 134.9)
- moved C601 342.2 mm to (305.9, 121.8), turned to 90 degrees
- moved TP501 332.3 mm to (251.3, 149.0)
- moved D204 332.3 mm to (240.9, 159.4), turned to 90 degrees
- moved TP503 329.8 mm to (253.5, 149.0)
- moved TP502 328.3 mm to (249.2, 149.0)
- moved H106 327.7 mm to (332.2, 152.6)
- moved BUZZER201 326.5 mm to (231.1, 157.9), turned to 90 degrees
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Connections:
- net Net-(D201-K) renamed /ESP32/YEL
- net Net-(D202-K) renamed /ESP32/GRN
- net Net-(D203-K) renamed /ESP32/RED
- net Net-(D601-K) renamed /PSU/INP_1
- net Net-(J805-Pin_3) renamed /AUX-CONNECTORS/CIPO
- C602 pad 1: +12V -> +5V
- C613 pad 1: /PSU/5V_SW -> /PSU/3V3_SW
- C615 pad 2: /PSU/5V_SW -> /PSU/3V3_SW
- C617 pad 1: /PSU/5V_SW -> /PSU/3V3_SW
- C619 pad 1: /PSU/5V_SW -> /PSU/3V3_SW
- C621 pad 1: /PSU/5V_SW -> /PSU/3V3_SW
- D601 pad 2: Net-(D601-A) -> /PSU/INP_2
- J413 pad 5: unconnected-(J413-Pin_5-Pad5) -> /BROTHER-CONNECTORS/ENC_BELTPHASE
- J601 pad 2: GND -> /PSU/INP_2
- J601 pad 3: (no net) -> /PSU/INP_2
- J802 pad 2: /AUX-CONNECTORS/I2C_VBUS -> /AUX-CONNECTORS/USER_I2C_VBUS
- J803 pad 3: /AUX-CONNECTORS/I2C_VBUS -> /AUX-CONNECTORS/USER_I2C_VBUS
- L602 pad 2: /PSU/5V_SW -> /PSU/3V3_SW
- R609 pad 2: /PSU/5V_SW -> /PSU/3V3_SW
- R610 pad 1: /PSU/5V_SW -> /PSU/3V3_SW
- R807 pad 1: /AUX-CONNECTORS/I2C_VBUS -> /AUX-CONNECTORS/USER_I2C_VBUS
- R808 pad 1: /AUX-CONNECTORS/I2C_VBUS -> /AUX-CONNECTORS/USER_I2C_VBUS
- SW201 pad 1: GND -> Net-(U201-SPIIO7/GPIO36/FSPICLK/SUBSPICLK)
- SW201 pad 2: Net-(U201-SPIIO7/GPIO36/FSPICLK/SUBSPICLK) -> GND
- TP603 pad 1: /PSU/5V_SW -> /PSU/3V3_SW
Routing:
- net +5V: track 15.4 -> 535.7 mm, vias 0 -> 21
- net +12V: track 0.00 -> 500.9 mm, vias 0 -> 1
- net +3V3: track 13.8 -> 457.3 mm, vias 0 -> 24
- net /BROTHER-CONNECTORS/EOL_R_N: track 21.1 -> 178.9 mm, vias 0 -> 2
- net /BROTHER-CONNECTORS/EOL_R_S: track 22.0 -> 177.2 mm, vias 0 -> 2
- net /AUX-CONNECTORS/AYAB_SCL: track 0.00 -> 139.5 mm
- net /AUX-CONNECTORS/AYAB_SDA: track 0.00 -> 136.9 mm
- net /IO CONDITIONING/EOL_L_L: track 21.0 -> 150.7 mm
- net /IO CONDITIONING/EOL_L_K: track 20.1 -> 143.0 mm
- net /ESP32/ESP14: track 0.00 -> 102.1 mm, vias 0 -> 1
- net /ESP32/ESP17: track 0.00 -> 100.7 mm, vias 0 -> 1
- net /ESP32/ESP18: track 0.00 -> 98.9 mm, vias 0 -> 1
- net /ESP32/ESP21: track 0.00 -> 98.4 mm, vias 0 -> 1
- net /ESP32/ESP39: track 0.00 -> 91.5 mm, vias 0 -> 1
- net /ESP32/ESP40: track 0.00 -> 88.6 mm, vias 0 -> 1
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- added copper zone on F.Cu, net /PSU/3V3_SW
- added copper zone on F.Cu, net /PSU/5V_SW
- added copper zone on B.Cu, net GND
- added copper zone on In1.Cu, net GND
- added copper zone on In2.Cu, net GND
- removed copper zone on F.Cu, net +3V3
- removed copper zone on F.Cu, net +5V
- removed copper zone on F.Cu, net Net-(D605-K)
- removed copper zone on F.Cu, net Net-(D606-K)
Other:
- board outline added: 300 x 48 mm
- copper layers 2 -> 4
- board text added: "14"
- board text added: "17"
- board text added: "18"
- board text added: "21"
- board text added: "39"
- board text added: "40"
- board text added: "41"
- board text added: "42"
- board text added: "c d + -"
- board text added: "github.com/AllYarnsAreBeautiful"
- board text added: "t r + -"

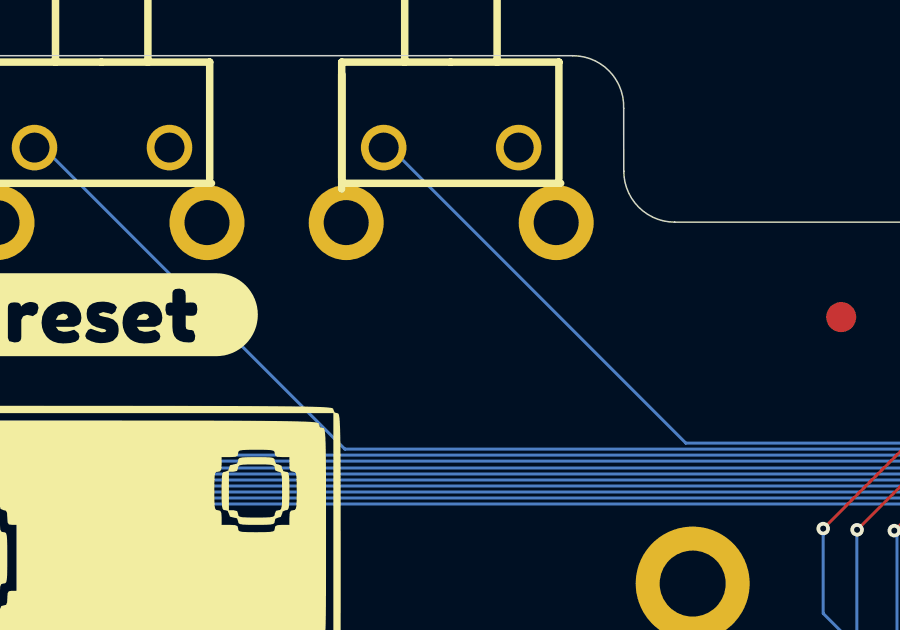
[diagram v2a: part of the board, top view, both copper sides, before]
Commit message: fix missing silk and remove temp files
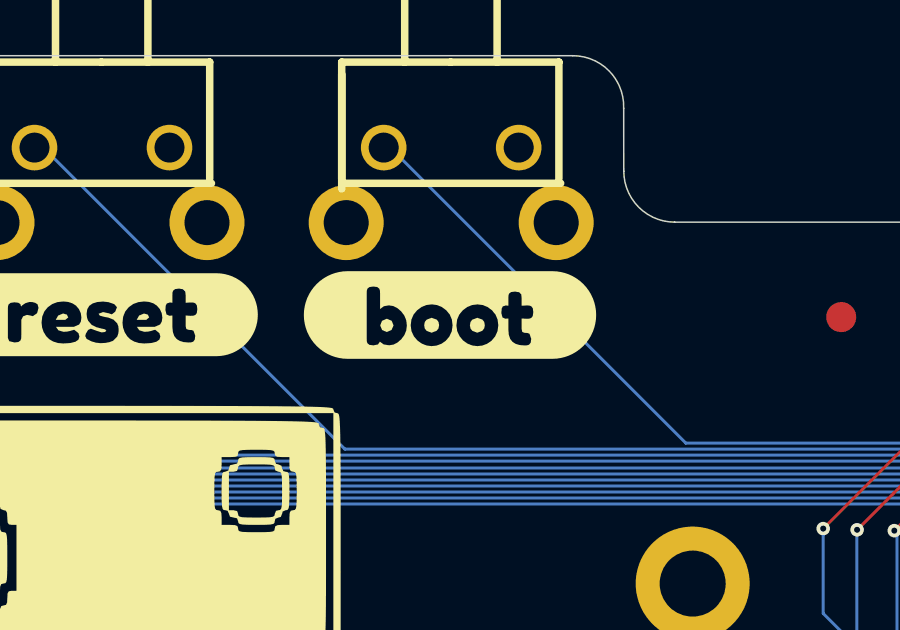
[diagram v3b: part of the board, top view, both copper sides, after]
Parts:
- added kibuzzard-65A40139: G***, kibuzzard-65A40139, F.Cu at (193.9, 124.8)
